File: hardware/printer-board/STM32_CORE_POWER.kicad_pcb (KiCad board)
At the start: 2 copper layers, 9 parts, among them J46 Conn_01x03, U14 AMS1117-3.3

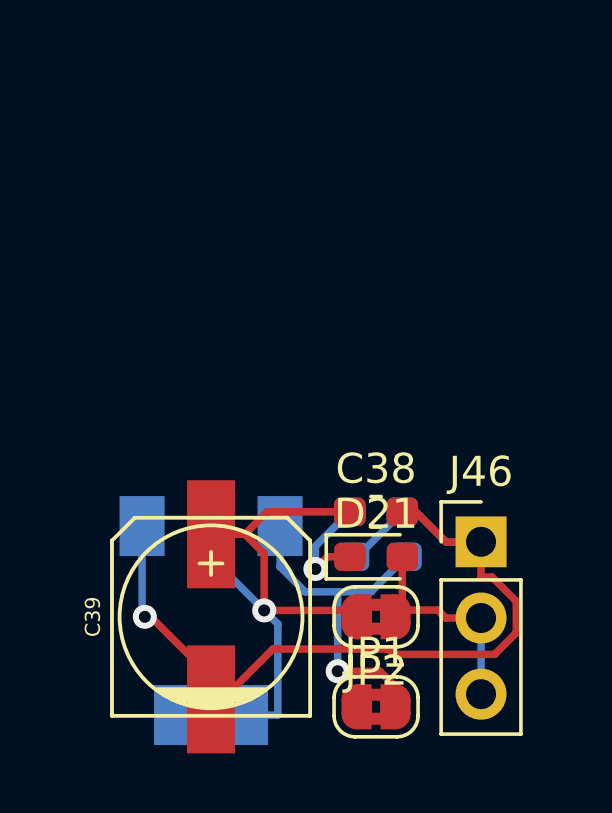
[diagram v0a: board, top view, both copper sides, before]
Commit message: update power circuit,
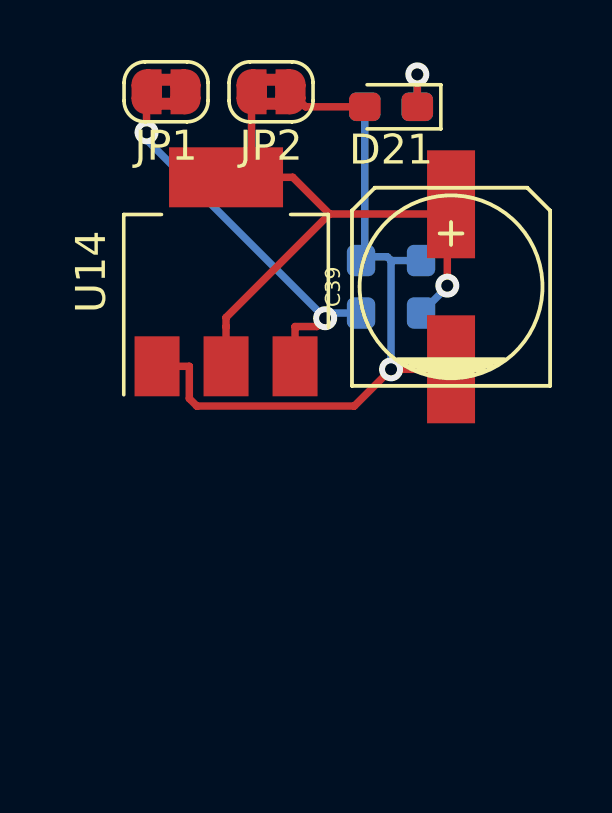
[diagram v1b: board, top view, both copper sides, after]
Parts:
- removed J46: Conn_01x03, Connector_PinHeader_2.54mm:PinHeader_1x03_P2.54mm_Vertical
- C38: moved to B.Cu
- D21: value LED_GREEN,0603 -> 3v3 HEALTHY
- U14: moved to F.Cu
- moved JP1 21.7 mm to (17.5, 16.5), turned to 180 degrees
- moved JP2 17.8 mm to (21.0, 16.5)
- moved D21 15.0 mm to (25.0, 17.0), turned to 180 degrees
- moved C39 13.6 mm to (27.0, 23.0)
- moved R65 13.5 mm to (25.0, 17.0), turned to 180 degrees
- moved U14 11.6 mm to (19.5, 22.5), turned to 90 degrees
- moved C37 9.02 mm to (24.0, 23.0), turned to 90 degrees
- moved C38 7.65 mm to (26.0, 23.0), turned to 90 degrees
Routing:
- net GND: track 30.3 -> 22.2 mm
- net +3V3: track 7.37 -> 2.68 mm
- net Net-(C37-Pad1): track 11.8 -> 13.7 mm, vias 1 -> 2
- net Net-(D21-Pad1): track 3.70 -> 2.16 mm
- net Net-(C38-Pad1): track 20.5 -> 21.4 mm

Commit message: update for stepper Z,
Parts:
- removed U14: AMS1117-3.3, Package_TO_SOT_SMD:SOT-223-3_TabPin2
- added C1: CP100uf,35V, Capacitor_SMD:C_0603_1608Metric_Pad1.05x0.95mm_HandSolder, F.Cu at (190.6, 45.3)
- added C10: CP100uf,25V, Capacitor_SMD:CP_Elec_6.3x7.7, F.Cu at (297.3, 53.2)
- added C11: C104,0603, Capacitor_SMD:C_0603_1608Metric_Pad1.05x0.95mm_HandSolder, F.Cu at (297.6, 59.1)
- added C12: CP100uf,25V, Capacitor_SMD:CP_Elec_6.3x7.7, F.Cu at (240.3, 109.1)
- added C13: C104,0603, Capacitor_SMD:C_0603_1608Metric_Pad1.05x0.95mm_HandSolder, F.Cu at (237.3, 115.0)
- added C14: C106,0603, Capacitor_SMD:C_0603_1608Metric_Pad1.05x0.95mm_HandSolder, F.Cu at (295.6, 127.7)
- added C15: C106,0603, Capacitor_SMD:C_0603_1608Metric_Pad1.05x0.95mm_HandSolder, F.Cu at (292.3, 136.8)
- added C16: C106,0603, Capacitor_SMD:C_0603_1608Metric_Pad1.05x0.95mm_HandSolder, F.Cu at (292.3, 127.7)
- added C17: C106,0603, Capacitor_SMD:C_0603_1608Metric_Pad1.05x0.95mm_HandSolder, F.Cu at (295.6, 129.2)
- added C18: C106,0603, Capacitor_SMD:C_0603_1608Metric_Pad1.05x0.95mm_HandSolder, F.Cu at (292.3, 132.3)
- added C19: C104,0603, Capacitor_SMD:C_0603_1608Metric_Pad1.05x0.95mm_HandSolder, F.Cu at (221.4, 140.3)
- added C2: CP100uf,25V, Capacitor_SMD:CP_Elec_6.3x7.7, F.Cu at (160.0, 109.1)
- added C20: CP100uf,35V, Capacitor_SMD:CP_Elec_6.3x7.7, F.Cu at (235.1, 137.6)
- added C21: C104,0603, Capacitor_SMD:C_0603_1608Metric_Pad1.05x0.95mm_HandSolder, F.Cu at (295.3, 86.0)
- added C22: C10pf,0603, Capacitor_SMD:C_0603_1608Metric_Pad1.05x0.95mm_HandSolder, F.Cu at (281.9, 85.8)
- added C23: C104,0603, Capacitor_SMD:C_0603_1608Metric_Pad1.05x0.95mm_HandSolder, F.Cu at (308.3, 76.8)
- added C24: C10pf,0603, Capacitor_SMD:C_0603_1608Metric_Pad1.05x0.95mm_HandSolder, F.Cu at (285.2, 85.8)
- added C25: C104,0603, Capacitor_SMD:C_0603_1608Metric_Pad1.05x0.95mm_HandSolder, F.Cu at (295.1, 82.0)
- added C26: C104,0603, Capacitor_SMD:C_0603_1608Metric_Pad1.05x0.95mm_HandSolder, F.Cu at (295.1, 80.4)
- added C27: C104,0603, Capacitor_SMD:C_0603_1608Metric_Pad1.05x0.95mm_HandSolder, F.Cu at (298.5, 80.4)
- added C28: C104,0603, Capacitor_SMD:C_0603_1608Metric_Pad1.05x0.95mm_HandSolder, F.Cu at (295.1, 83.5)
- added C29: C105,0603, Capacitor_SMD:C_0603_1608Metric_Pad1.05x0.95mm_HandSolder, F.Cu at (305.0, 75.3)
- added C3: C104,0603, Capacitor_SMD:C_0603_1608Metric_Pad1.05x0.95mm_HandSolder, F.Cu at (166.4, 109.9)
- added C30: C104,0603, Capacitor_SMD:C_0603_1608Metric_Pad1.05x0.95mm_HandSolder, F.Cu at (298.5, 78.9)
- added C31: C104,0603, Capacitor_SMD:C_0603_1608Metric_Pad1.05x0.95mm_HandSolder, F.Cu at (291.9, 85.8)
- added C32: C104,0603, Capacitor_SMD:C_0603_1608Metric_Pad1.05x0.95mm_HandSolder, F.Cu at (288.6, 85.8)
- added C33: CP220uf,16V, Capacitor_SMD:C_0603_1608Metric_Pad1.05x0.95mm_HandSolder, F.Cu at (147.7, 149.0)
- added C34: CP220uf,16V, Capacitor_SMD:C_0603_1608Metric_Pad1.05x0.95mm_HandSolder, F.Cu at (144.3, 149.0)
- added C35: CP220uf,25V, Capacitor_SMD:C_0603_1608Metric_Pad1.05x0.95mm_HandSolder, F.Cu at (144.3, 150.5)
- added C36: CP100uf,16V, Capacitor_SMD:CP_Elec_6.3x5.3, F.Cu at (259.2, 130.5)
- added C4: CP100uf,25V, Capacitor_SMD:CP_Elec_6.3x7.7, F.Cu at (200.2, 109.1)
- added C40: C104,0603, Capacitor_SMD:C_0603_1608Metric_Pad1.05x0.95mm_HandSolder, F.Cu at (254.2, 84.5)
- added C41: CP100uf,25V, Capacitor_SMD:CP_Elec_6.3x7.7, F.Cu at (257.2, 53.2)
- added C42: C104,0603, Capacitor_SMD:C_0603_1608Metric_Pad1.05x0.95mm_HandSolder, F.Cu at (263.6, 54.0)
- added C43: C104,0603, Capacitor_SMD:C_0603_1608Metric_Pad1.05x0.95mm_HandSolder, F.Cu at (274.0, 103.0)
- added C44: CP100uf,16V, Capacitor_SMD:CP_Elec_6.3x5.3, F.Cu at (280.3, 95.8)
- added C45: C106,0603, Capacitor_SMD:C_0603_1608Metric_Pad1.05x0.95mm_HandSolder, F.Cu at (318.6, 92.3)
- added C46: C104,0603, Capacitor_SMD:C_0603_1608Metric_Pad1.05x0.95mm_HandSolder, F.Cu at (325.3, 92.3)
- added C47: C332,0603, Capacitor_SMD:C_0603_1608Metric_Pad1.05x0.95mm_HandSolder, F.Cu at (322.0, 92.3)
- added C48: C103,0603, Capacitor_SMD:C_0603_1608Metric_Pad1.05x0.95mm_HandSolder, F.Cu at (318.6, 93.8)
- added C49: C226,6.3v,0603, Capacitor_SMD:C_0603_1608Metric_Pad1.05x0.95mm_HandSolder, F.Cu at (328.7, 93.8)
- added C5: C104,0603, Capacitor_SMD:C_0603_1608Metric_Pad1.05x0.95mm_HandSolder, F.Cu at (197.2, 116.6)
- added C50: C106,0603, Capacitor_SMD:C_0603_1608Metric_Pad1.05x0.95mm_HandSolder, F.Cu at (224.8, 152.9)
- added C51: C104,0603, Capacitor_SMD:C_0603_1608Metric_Pad1.05x0.95mm_HandSolder, F.Cu at (228.1, 151.4)
- added C52: C332,0603, Capacitor_SMD:C_0603_1608Metric_Pad1.05x0.95mm_HandSolder, F.Cu at (221.4, 152.9)
- added C53: C103,0603, Capacitor_SMD:C_0603_1608Metric_Pad1.05x0.95mm_HandSolder, F.Cu at (224.8, 151.4)
- added C54: C226,6.3v,0603, Capacitor_SMD:C_0603_1608Metric_Pad1.05x0.95mm_HandSolder, F.Cu at (221.4, 151.4)
- added C6: CP100uf,25V, Capacitor_SMD:CP_Elec_6.3x7.7, F.Cu at (160.0, 133.1)
- added C7: C104,0603, Capacitor_SMD:C_0603_1608Metric_Pad1.05x0.95mm_HandSolder, F.Cu at (160.3, 139.0)
- added C8: CP100uf,25V, Capacitor_SMD:CP_Elec_6.3x7.7, F.Cu at (200.1, 133.1)
- added C9: C104,0603, Capacitor_SMD:C_0603_1608Metric_Pad1.05x0.95mm_HandSolder, F.Cu at (197.1, 140.5)
- added D1: 5V HEALTHY, LED_SMD:LED_0603_1608Metric_Pad1.05x0.95mm_HandSolder, F.Cu at (141.2, 93.6)
- added D10: LED_BLUE,0603, LED_SMD:LED_0603_1608Metric_Pad1.05x0.95mm_HandSolder, F.Cu at (315.2, 79.3)
- added D11: LED_BLUE,0603, LED_SMD:LED_0603_1608Metric_Pad1.05x0.95mm_HandSolder, F.Cu at (318.6, 79.3)
- added D12: LED_BLUE,0603, LED_SMD:LED_0603_1608Metric_Pad1.05x0.95mm_HandSolder, F.Cu at (318.6, 80.9)
- added D13: LED_BLUE,0603, LED_SMD:LED_0603_1608Metric_Pad1.05x0.95mm_HandSolder, F.Cu at (325.4, 79.3)
- added D14: LED_BLUE,0603, LED_SMD:LED_0603_1608Metric_Pad1.05x0.95mm_HandSolder, F.Cu at (322.0, 79.3)
- added D15: SD_M4, Diode_SMD:D_SOD-323_HandSoldering, F.Cu at (221.8, 136.1)
- added D16: SD_M4, Diode_SMD:D_SOD-323_HandSoldering, F.Cu at (225.8, 136.1)
- added D17: PB9, LED_SMD:LED_0603_1608Metric_Pad1.05x0.95mm_HandSolder, F.Cu at (278.5, 85.8)
- added D18: LED_RED,0603, LED_SMD:LED_0603_1608Metric_Pad1.05x0.95mm_HandSolder, F.Cu at (295.3, 102.5)
- added D19: LED_RED,0603, LED_SMD:LED_0603_1608Metric_Pad1.05x0.95mm_HandSolder, F.Cu at (265.4, 122.5)
- added D2: LED_BLUE,0603, LED_SMD:LED_0603_1608Metric_Pad1.05x0.95mm_HandSolder, F.Cu at (157.0, 115.4)
- added D20: LED_BLUE,0603, LED_SMD:LED_0603_1608Metric_Pad1.05x0.95mm_HandSolder, F.Cu at (259.8, 134.9)
- added D22: LED_BLUE,0603, LED_SMD:LED_0603_1608Metric_Pad1.05x0.95mm_HandSolder, F.Cu at (272.1, 142.3)
- added D23: LED_BLUE,0603, LED_SMD:LED_0603_1608Metric_Pad1.05x0.95mm_HandSolder, F.Cu at (254.2, 81.4)
- added D24: LED_BLUE,0603, LED_SMD:LED_0603_1608Metric_Pad1.05x0.95mm_HandSolder, F.Cu at (254.2, 57.5)
- added D3: LED_BLUE,0603, LED_SMD:LED_0603_1608Metric_Pad1.05x0.95mm_HandSolder, F.Cu at (197.2, 113.5)
- added D4: LED_BLUE,0603, LED_SMD:LED_0603_1608Metric_Pad1.05x0.95mm_HandSolder, F.Cu at (157.0, 137.4)
- added D5: LED_BLUE,0603, LED_SMD:LED_0603_1608Metric_Pad1.05x0.95mm_HandSolder, F.Cu at (197.1, 137.4)
- added D6: LED_BLUE,0603, LED_SMD:LED_0603_1608Metric_Pad1.05x0.95mm_HandSolder, F.Cu at (294.3, 57.5)
- added D7: LED_BLUE,0603, LED_SMD:LED_0603_1608Metric_Pad1.05x0.95mm_HandSolder, F.Cu at (237.3, 113.5)
- added D8: LED_RED,0603, LED_SMD:LED_0603_1608Metric_Pad1.05x0.95mm_HandSolder, F.Cu at (295.3, 119.1)
- added D9: LED_BLUE,0603, LED_SMD:LED_0603_1608Metric_Pad1.05x0.95mm_HandSolder, F.Cu at (315.2, 80.9)
- added F1: 16V/30A, w_misc_comp:fuse_smf, F.Cu at (225.0, 127.0)
- added F2: 30V/5A, w_misc_comp:fuse_smf, F.Cu at (225.0, 132.4)
- added H1: MOUNT_M3, MountingHole:MountingHole_2.7mm_M2.5, F.Cu at (3.00, 3.00)
- added H2: MOUNT_M3, MountingHole:MountingHole_2.7mm_M2.5, F.Cu at (97.0, 3.00)
- added H3: MOUNT_M3, MountingHole:MountingHole_2.7mm_M2.5, F.Cu at (3.00, 97.0)
- added H4: MOUNT_M3, MountingHole:MountingHole_2.7mm_M2.5, F.Cu at (97.0, 97.0)
- added J1: USB_DEBUG, Connector_PinHeader_1.27mm:PinHeader_1x05_P1.27mm_Vertical, F.Cu at (187.4, 45.7)
- added J10: MS_SELECT, Connector_PinHeader_2.54mm:PinHeader_2x03_P2.54mm_Vertical, F.Cu at (304.8, 46.3)
- added J11: E0, footprint-lib:b4b-ph-kl,stepper_terminal, F.Cu at (297.8, 46.6)
- added J12: MS_SELECT, Connector_PinHeader_2.54mm:PinHeader_2x03_P2.54mm_Vertical, F.Cu at (247.8, 102.3)
- added J13: E1, footprint-lib:b4b-ph-kl,stepper_terminal, F.Cu at (240.8, 102.6)
- added J14: HEATBED, footprint-lib:mpt_0,5%2f2-2,54,heatbed, F.Cu at (309.5, 113.4)
- added J15: X_MIN, footprint-lib:b3b-ph-kl,end_stop, F.Cu at (317.7, 70.5)
- added J16: X_MAX, footprint-lib:b3b-ph-kl,end_stop, F.Cu at (317.7, 75.6)
- added J17: Y_MIN, footprint-lib:b3b-ph-kl,end_stop, F.Cu at (326.1, 70.5)
- added J18: Y_MAX, footprint-lib:b3b-ph-kl,end_stop, F.Cu at (326.1, 75.6)
- added J19: Z_MIN, footprint-lib:b3b-ph-kl,end_stop, F.Cu at (334.5, 70.5)
- added J2: MS_SELECT, Connector_PinHeader_2.54mm:PinHeader_2x03_P2.54mm_Vertical, F.Cu at (167.5, 102.3)
- added J20: Z_MAX, footprint-lib:b3b-ph-kl,end_stop, F.Cu at (334.5, 75.6)
- added J21: HEATBED_TEMP, w_conn_jst-ph:b2b-ph-kl, F.Cu at (281.1, 134.1)
- added J22: HOTEND_TEMP0, w_conn_jst-ph:b2b-ph-kl, F.Cu at (281.1, 129.1)
- added J23: HOTEND_TEMP1, w_conn_jst-ph:b2b-ph-kl, F.Cu at (287.4, 129.1)
- added J24: AUX_TEMP, w_conn_jst-ph:b2b-ph-kl, F.Cu at (287.4, 134.1)
- added J25: 12V_INPUT_2, footprint-lib:mpt_0,5%2f2-2,54,12V_SRC, F.Cu at (245.3, 130.8)
- added J26: 12V_INPUT, footprint-lib:mpt_0,5%2f2-2,54,12V_SRC, F.Cu at (239.3, 130.8)
- added J27: 12V_OUT, footprint-lib:mpt_0,5%2f2-2,54,12V_SRC, F.Cu at (233.3, 130.8)
- added J28: SWD, Connector_PinHeader_1.27mm:PinHeader_1x04_P1.27mm_Vertical, F.Cu at (307.2, 69.6)
- added J29: USB_DEBUG, Connector_PinHeader_1.27mm:PinHeader_1x05_P1.27mm_Vertical, F.Cu at (157.4, 149.5)
- added J3: X, footprint-lib:b4b-ph-kl,stepper_terminal, F.Cu at (160.5, 102.6)
- added J30: PWR_DEBUG, Connector_PinHeader_1.27mm:PinHeader_1x05_P1.27mm_Vertical, F.Cu at (141.1, 149.5)
- added J31: HOT_END, footprint-lib:mpt_0,5%2f2-2,54,heatbed, F.Cu at (309.5, 96.8)
- added J32: HOT_END, footprint-lib:mpt_0,5%2f2-2,54,heatbed, F.Cu at (279.6, 116.8)
- added J33: TO FAN0, footprint-lib:b2b-ph-kl,fan_pwm_out, F.Cu at (267.2, 129.1)
- added J34: TO FAN1, footprint-lib:b2b-ph-kl,fan_pwm_out, F.Cu at (329.8, 46.6)
- added J35: TO FAN2, footprint-lib:b2b-ph-kl,fan_pwm_out, F.Cu at (267.2, 143.6)
- added J36: MS_SELECT, Connector_PinHeader_2.54mm:PinHeader_2x03_P2.54mm_Vertical, F.Cu at (264.7, 70.2)
- added J37: Z2, footprint-lib:b4b-ph-kl,stepper_terminal, F.Cu at (257.7, 70.5)
- added J38: MS_SELECT, Connector_PinHeader_2.54mm:PinHeader_2x03_P2.54mm_Vertical, F.Cu at (264.7, 46.3)
- added J39: Y, footprint-lib:b4b-ph-kl,stepper_terminal, F.Cu at (257.7, 46.6)
- added J4: MS_SELECT, Connector_PinHeader_2.54mm:PinHeader_2x03_P2.54mm_Vertical, F.Cu at (207.7, 102.3)
- added J40: Conn_01x07, Connector_PinHeader_1.27mm:PinHeader_1x07_P1.27mm_Vertical, F.Cu at (273.9, 93.4)
- added J41: EXP1, Connector_PinHeader_2.54mm:PinHeader_2x05_P2.54mm_Vertical, F.Cu at (261.8, 94.1)
- added J42: EXP2, Connector_PinHeader_2.54mm:PinHeader_2x05_P2.54mm_Vertical, F.Cu at (268.0, 94.1)
- added J5: Z, footprint-lib:b4b-ph-kl,stepper_terminal, F.Cu at (200.7, 102.6)
- added J6: MS_SELECT, Connector_PinHeader_2.54mm:PinHeader_2x03_P2.54mm_Vertical, F.Cu at (167.5, 126.2)
- added J7: Z1, footprint-lib:b4b-ph-kl,stepper_terminal, F.Cu at (160.5, 126.5)
- added J8: MS_SELECT, Connector_PinHeader_2.54mm:PinHeader_2x03_P2.54mm_Vertical, F.Cu at (207.6, 126.2)
- added J9: Z3, footprint-lib:b4b-ph-kl,stepper_terminal, F.Cu at (200.6, 126.5)
- added JP3: Jumper_NO_Small, Jumper:SolderJumper-2_P1.3mm_Open_TrianglePad1.0x1.5mm, F.Cu at (194.0, 45.8)
- added JP4: Jumper_NO_Small, Jumper:SolderJumper-2_P1.3mm_Open_TrianglePad1.0x1.5mm, F.Cu at (144.6, 94.1)
- added JP5: Jumper_NO_Small, SolderJumper-2_P1.3mm_Open_TrianglePad1.0x1.5mm, F.Cu at (221.4, 138.3)
- added JP6: Jumper_NO_Small, SolderJumper-2_P1.3mm_Open_TrianglePad1.0x1.5mm, F.Cu at (298.5, 84.0)
- added JP7: Jumper_NO_Small, SolderJumper-2_P1.3mm_Open_TrianglePad1.0x1.5mm, F.Cu at (305.2, 78.8)
- added L1: L_Small, w_smd_inductors:inductor_smd_0603, F.Cu at (301.3, 83.4)
- added L2: L_15uH, w_smd_inductors:inductor_smd_4.8x2.8mm, F.Cu at (327.2, 88.8)
- added L3: L_15uH, w_smd_inductors:inductor_smd_4.8x2.8mm, F.Cu at (229.9, 147.9)
- added Q1: WSK220N04, footprint-lib:TO-263-2,drill_array, F.Cu at (298.1, 112.6)
- added Q2: STP55NF06, footprint-lib:TO-263-2,drill_array, F.Cu at (298.1, 96.0)
- added Q3: STP55NF06, footprint-lib:TO-263-2,drill_array, F.Cu at (268.3, 116.0)
- added Q4: D882, footprint-lib:SOT-89-3,thermal_vias, F.Cu at (266.5, 134.6)
- added Q5: D882, footprint-lib:SOT-89-3,thermal_vias, F.Cu at (329.1, 52.2)
- added Q6: D882, footprint-lib:SOT-89-3,thermal_vias, F.Cu at (266.5, 149.2)
- added R1: R153,0603, Resistor_SMD:R_0603_1608Metric_Pad1.05x0.95mm_HandSolder, F.Cu at (238.4, 94.5)
- added R10: R103,0603, Resistor_SMD:R_0603_1608Metric_Pad1.05x0.95mm_HandSolder, F.Cu at (160.4, 115.4)
- added R11: R104,0603, Resistor_SMD:R_0603_1608Metric_Pad1.05x0.95mm_HandSolder, F.Cu at (197.2, 115.0)
- added R12: R102,0603, Resistor_SMD:R_0603_1608Metric_Pad1.05x0.95mm_HandSolder, F.Cu at (206.6, 109.9)
- added R13: R103,0603, Resistor_SMD:R_0603_1608Metric_Pad1.05x0.95mm_HandSolder, F.Cu at (200.5, 115.0)
- added R14: R104,0603, Resistor_SMD:R_0603_1608Metric_Pad1.05x0.95mm_HandSolder, F.Cu at (166.4, 133.9)
- added R15: R102,0603, Resistor_SMD:R_0603_1608Metric_Pad1.05x0.95mm_HandSolder, F.Cu at (157.0, 139.0)
- added R16: R103,0603, Resistor_SMD:R_0603_1608Metric_Pad1.05x0.95mm_HandSolder, F.Cu at (157.0, 140.5)
- added R17: R104,0603, Resistor_SMD:R_0603_1608Metric_Pad1.05x0.95mm_HandSolder, F.Cu at (197.1, 139.0)
- added R18: R102,0603, Resistor_SMD:R_0603_1608Metric_Pad1.05x0.95mm_HandSolder, F.Cu at (206.5, 133.9)
- added R19: R103,0603, Resistor_SMD:R_0603_1608Metric_Pad1.05x0.95mm_HandSolder, F.Cu at (200.4, 139.0)
- added R2: R153,0603, Resistor_SMD:R_0603_1608Metric_Pad1.05x0.95mm_HandSolder, F.Cu at (238.4, 93.0)
- added R20: R104,0603, Resistor_SMD:R_0603_1608Metric_Pad1.05x0.95mm_HandSolder, F.Cu at (303.7, 54.0)
- added R21: R102,0603, Resistor_SMD:R_0603_1608Metric_Pad1.05x0.95mm_HandSolder, F.Cu at (294.3, 60.6)
- added R22: R103,0603, Resistor_SMD:R_0603_1608Metric_Pad1.05x0.95mm_HandSolder, F.Cu at (294.3, 59.1)
- added R23: R104,0603, Resistor_SMD:R_0603_1608Metric_Pad1.05x0.95mm_HandSolder, F.Cu at (240.6, 115.0)
- added R24: R102,0603, Resistor_SMD:R_0603_1608Metric_Pad1.05x0.95mm_HandSolder, F.Cu at (246.7, 109.9)
- added R25: R103,0603, Resistor_SMD:R_0603_1608Metric_Pad1.05x0.95mm_HandSolder, F.Cu at (237.3, 116.6)
- added R26: R100,0805, Resistor_SMD:R_0805_2012Metric_Pad1.15x1.40mm_HandSolder, F.Cu at (308.3, 117.6)
- added R27: R104,0805, Resistor_SMD:R_0805_2012Metric_Pad1.15x1.40mm_HandSolder, F.Cu at (291.7, 119.3)
- added R28: R182,0603, Resistor_SMD:R_0603_1608Metric_Pad1.05x0.95mm_HandSolder, F.Cu at (298.6, 119.0)
- added R29: R102,0603, Resistor_SMD:R_0603_1608Metric_Pad1.05x0.95mm_HandSolder, F.Cu at (332.0, 82.3)
- added R3: R152,0603, Resistor_SMD:R_0603_1608Metric_Pad1.05x0.95mm_HandSolder, F.Cu at (241.7, 93.0)
- added R30: R102,0603, Resistor_SMD:R_0603_1608Metric_Pad1.05x0.95mm_HandSolder, F.Cu at (328.7, 79.3)
- added R31: R102,0603, Resistor_SMD:R_0603_1608Metric_Pad1.05x0.95mm_HandSolder, F.Cu at (325.3, 80.9)
- added R32: R102,0603, Resistor_SMD:R_0603_1608Metric_Pad1.05x0.95mm_HandSolder, F.Cu at (328.7, 80.8)
- added R33: R102,0603, Resistor_SMD:R_0603_1608Metric_Pad1.05x0.95mm_HandSolder, F.Cu at (328.7, 82.3)
- added R34: R102,0603, Resistor_SMD:R_0603_1608Metric_Pad1.05x0.95mm_HandSolder, F.Cu at (322.0, 80.9)
- added R35: R472,0603, Resistor_SMD:R_0603_1608Metric_Pad1.05x0.95mm_HandSolder, F.Cu at (292.3, 129.2)
- added R36: R472,0603, Resistor_SMD:R_0603_1608Metric_Pad1.05x0.95mm_HandSolder, F.Cu at (292.3, 130.7)
- added R37: R472,0603, Resistor_SMD:R_0603_1608Metric_Pad1.05x0.95mm_HandSolder, F.Cu at (292.3, 135.3)
- added R38: R472,0603, Resistor_SMD:R_0603_1608Metric_Pad1.05x0.95mm_HandSolder, F.Cu at (295.6, 132.3)
- added R39: R472,0603, Resistor_SMD:R_0603_1608Metric_Pad1.05x0.95mm_HandSolder, F.Cu at (292.3, 133.8)
- added R4: R220,0603, Resistor_SMD:R_0603_1608Metric_Pad1.05x0.95mm_HandSolder, F.Cu at (187.5, 52.7)
- added R40: R472,0603, Resistor_SMD:R_0603_1608Metric_Pad1.05x0.95mm_HandSolder, F.Cu at (301.8, 82.0)
- added R41: R472,0603, Resistor_SMD:R_0603_1608Metric_Pad1.05x0.95mm_HandSolder, F.Cu at (301.8, 80.4)
- added R42: R0,0603, Resistor_SMD:R_0603_1608Metric_Pad1.05x0.95mm_HandSolder, F.Cu at (308.3, 75.3)
- added R43: R0,0603, Resistor_SMD:R_0603_1608Metric_Pad1.05x0.95mm_HandSolder, F.Cu at (295.1, 78.9)
- added R44: R102,0603, Resistor_SMD:R_0603_1608Metric_Pad1.05x0.95mm_HandSolder, F.Cu at (301.8, 78.9)
- added R45: R103,0603, Resistor_SMD:R_0603_1608Metric_Pad1.05x0.95mm_HandSolder, F.Cu at (305.0, 76.8)
- added R46: R103,0603, Resistor_SMD:R_0603_1608Metric_Pad1.05x0.95mm_HandSolder, F.Cu at (298.5, 82.0)
- added R47: R220,0603, Resistor_SMD:R_0603_1608Metric_Pad1.05x0.95mm_HandSolder, F.Cu at (160.7, 150.5)
- added R48: R220,0603, Resistor_SMD:R_0603_1608Metric_Pad1.05x0.95mm_HandSolder, F.Cu at (164.0, 149.0)
- added R49: R152,0603, Resistor_SMD:R_0603_1608Metric_Pad1.05x0.95mm_HandSolder, F.Cu at (160.7, 149.0)
- added R5: R220,0603, Resistor_SMD:R_0603_1608Metric_Pad1.05x0.95mm_HandSolder, F.Cu at (147.9, 93.6)
- added R50: R100,0805, Resistor_SMD:R_0805_2012Metric_Pad1.15x1.40mm_HandSolder, F.Cu at (308.3, 101.0)
- added R51: R104,0805, Resistor_SMD:R_0805_2012Metric_Pad1.15x1.40mm_HandSolder, F.Cu at (291.7, 102.7)
- added R52: R182,0603, Resistor_SMD:R_0603_1608Metric_Pad1.05x0.95mm_HandSolder, F.Cu at (298.6, 102.4)
- added R53: R100,0805, Resistor_SMD:R_0805_2012Metric_Pad1.15x1.40mm_HandSolder, F.Cu at (261.8, 122.7)
- added R54: R104,0805, Resistor_SMD:R_0805_2012Metric_Pad1.15x1.40mm_HandSolder, F.Cu at (278.5, 121.0)
- added R55: R182,0603, Resistor_SMD:R_0603_1608Metric_Pad1.05x0.95mm_HandSolder, F.Cu at (268.8, 122.5)
- added R56: R100,0805, Resistor_SMD:R_0805_2012Metric_Pad1.15x1.40mm_HandSolder, F.Cu at (272.3, 127.9)
- added R57: R104,0805, Resistor_SMD:R_0805_2012Metric_Pad1.15x1.40mm_HandSolder, F.Cu at (256.2, 135.1)
- added R58: R100,0603, Resistor_SMD:R_0603_1608Metric_Pad1.05x0.95mm_HandSolder, F.Cu at (259.4, 136.8)
- added R59: R182,0603, Resistor_SMD:R_0603_1608Metric_Pad1.05x0.95mm_HandSolder, F.Cu at (256.0, 136.8)
- added R6: R152,0603, Resistor_SMD:R_0603_1608Metric_Pad1.05x0.95mm_HandSolder, F.Cu at (190.6, 48.3)
- added R60: R100,0805, Resistor_SMD:R_0805_2012Metric_Pad1.15x1.40mm_HandSolder, F.Cu at (334.8, 45.5)
- added R61: R104,0805, Resistor_SMD:R_0805_2012Metric_Pad1.15x1.40mm_HandSolder, F.Cu at (318.8, 52.6)
- added R62: R100,0603, Resistor_SMD:R_0603_1608Metric_Pad1.05x0.95mm_HandSolder, F.Cu at (318.6, 54.4)
- added R63: R182,0603, Resistor_SMD:R_0603_1608Metric_Pad1.05x0.95mm_HandSolder, F.Cu at (322.0, 54.4)
- added R64: R100,0805, Resistor_SMD:R_0603_1608Metric_Pad1.05x0.95mm_HandSolder, F.Cu at (259.8, 149.4)
- added R66: R100,0603, Resistor_SMD:R_0603_1608Metric_Pad1.05x0.95mm_HandSolder, F.Cu at (256.0, 151.4)
- added R67: R182,0603, Resistor_SMD:R_0603_1608Metric_Pad1.05x0.95mm_HandSolder, F.Cu at (259.4, 151.4)
- added R68: R104,0603, Resistor_SMD:R_0603_1608Metric_Pad1.05x0.95mm_HandSolder, F.Cu at (257.5, 83.0)
- added R69: R102,0603, Resistor_SMD:R_0603_1608Metric_Pad1.05x0.95mm_HandSolder, F.Cu at (254.2, 83.0)
- added R7: R102,0603, Resistor_SMD:R_0603_1608Metric_Pad1.05x0.95mm_HandSolder, F.Cu at (190.6, 46.8)
- added R70: R103,0603, Resistor_SMD:R_0603_1608Metric_Pad1.05x0.95mm_HandSolder, F.Cu at (263.6, 77.8)
- added R71: R104,0603, Resistor_SMD:R_0603_1608Metric_Pad1.05x0.95mm_HandSolder, F.Cu at (257.5, 59.1)
- added R72: R102,0603, Resistor_SMD:R_0603_1608Metric_Pad1.05x0.95mm_HandSolder, F.Cu at (254.2, 60.6)
- added R73: R103,0603, Resistor_SMD:R_0603_1608Metric_Pad1.05x0.95mm_HandSolder, F.Cu at (254.2, 59.1)
- added R74: R562,0603, Resistor_SMD:R_0603_1608Metric_Pad1.05x0.95mm_HandSolder, F.Cu at (328.7, 92.3)
- added R75: R103,0603, Resistor_SMD:R_0603_1608Metric_Pad1.05x0.95mm_HandSolder, F.Cu at (325.3, 93.8)
- added R76: R333,0603, Resistor_SMD:R_0603_1608Metric_Pad1.05x0.95mm_HandSolder, F.Cu at (322.0, 93.8)
- added R77: R562,0603, Resistor_SMD:R_0603_1608Metric_Pad1.05x0.95mm_HandSolder, F.Cu at (228.1, 152.9)
- added R78: R103,0603, Resistor_SMD:R_0603_1608Metric_Pad1.05x0.95mm_HandSolder, F.Cu at (231.5, 151.4)
- added R79: R333,0603, Resistor_SMD:R_0603_1608Metric_Pad1.05x0.95mm_HandSolder, F.Cu at (231.5, 152.9)
- added R8: R104,0603, Resistor_SMD:R_0805_2012Metric_Pad1.15x1.40mm_HandSolder, F.Cu at (157.2, 113.7)
- added R9: R102,0603, Resistor_SMD:R_0603_1608Metric_Pad1.05x0.95mm_HandSolder, F.Cu at (157.0, 117.0)
- added SW1: SW_Push, Button_Switch_SMD:SW_SPST_CK_RS282G05A3, F.Cu at (298.4, 76.1)
- added TH1: Thermistor_NTC, Resistor_SMD:R_0603_1608Metric_Pad1.05x0.95mm_HandSolder, F.Cu at (295.6, 130.7)
- added U1: orange_pi_zero, footprint-lib:orangepi-zero, F.Cu at (139.8, 92.6)
- added U10: A4988_MODULE, footprint-lib:Pololu_Breakout-16_15.2x20.3mm, F.Cu at (238.2, 46.0)
- added U11: MP2303A_ALT, footprint-lib:SOIC-8_3.9x4.9mm_P1.27mm,thermal_via, F.Cu at (320.7, 88.8)
- added U12: MP2303A_ALT, footprint-lib:SOIC-8_3.9x4.9mm_P1.27mm,thermal_via, F.Cu at (223.5, 147.9)
- added U2: A4988_MODULE, footprint-lib:Pololu_Breakout-16_15.2x20.3mm, F.Cu at (141.1, 102.0)
- added U3: A4988_MODULE, footprint-lib:Pololu_Breakout-16_15.2x20.3mm, F.Cu at (181.3, 102.0)
- added U4: A4988_MODULE, footprint-lib:Pololu_Breakout-16_15.2x20.3mm, F.Cu at (141.1, 125.9)
- added U5: A4988_MODULE, footprint-lib:Pololu_Breakout-16_15.2x20.3mm, F.Cu at (181.2, 125.9)
- added U6: A4988_MODULE, footprint-lib:Pololu_Breakout-16_15.2x20.3mm, F.Cu at (278.4, 46.0)
- added U7: A4988_MODULE, footprint-lib:Pololu_Breakout-16_15.2x20.3mm, F.Cu at (221.4, 102.0)
- added U8: STM32F407VET6, w_smd_lqfp:TQFP-100, F.Cu at (285.1, 76.7)
- added U9: A4988_MODULE, footprint-lib:Pololu_Breakout-16_15.2x20.3mm, F.Cu at (238.2, 69.9)
- added Y1: O_8M, Crystal:Crystal_HC49-4H_Vertical, F.Cu at (297.1, 71.2)
- C37, C38: value C104,0603 -> CP100uf,16V; footprint Capacitor_SMD:C_0603_1608Metric_Pad1.05x0.95mm_HandSolder -> Capacitor_SMD:CP_Elec_6.3x5.3; moved to F.Cu
- C39: value CP47uf,50V -> CP100uf,25V; footprint w_smd_cap:c_elec_6.3x7.7 -> Capacitor_SMD:CP_Elec_6.3x7.7
- D21: value 3v3 HEALTHY -> LED_BLUE,0603
- JP1, JP2: footprint Jumper:SolderJumper-2_P1.3mm_Bridged2Bar_RoundedPad1.0x1.5mm -> Jumper:SolderJumper-2_P1.3mm_Open_TrianglePad1.0x1.5mm
- R65: value R102,0603 -> R104,0805; footprint Resistor_SMD:R_0603_1608Metric_Pad1.05x0.95mm_HandSolder -> Resistor_SMD:R_0805_2012Metric_Pad1.15x1.40mm_HandSolder; moved to F.Cu
- moved D21 299.5 mm to (322.4, 52.4), turned to 0 degrees
- moved C37 298.8 mm to (321.8, 48.1), turned to 0 degrees
- moved R65 266.6 mm to (256.2, 149.6), turned to 0 degrees
- moved C38 263.2 mm to (259.2, 145.1), turned to 0 degrees
- moved C39 236.5 mm to (257.2, 77.0), turned to 0 degrees
- moved JP2 170.8 mm to (187.5, 54.7), turned to 0 degrees
- moved JP1 146.9 mm to (141.2, 95.7), turned to 0 degrees
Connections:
- C37 pad 1: Net-(C37-Pad1) -> +12V
- C38 pad 1: Net-(C38-Pad1) -> +12V
- C39 pad 1: Net-(C38-Pad1) -> +12V
- D21 pad 2: +3V3 -> Net-(D21-Pad2)
- JP1 pad 1: +5V -> /orange_pi/OPI_USB-DM2
- JP1 pad 2: Net-(C37-Pad1) -> /orange_pi/USB-DM2
- JP2 pad 1: +3V3 -> /orange_pi/OPI_USB-DP2
- JP2 pad 2: Net-(C38-Pad1) -> /orange_pi/USB-DP2
- R65 pad 1: Net-(D21-Pad1) -> GND
- R65 pad 2: GND -> /FANS/FAN2/FAN_EN
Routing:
- net GND: track 22.2 -> 0.00 mm, vias 1 -> 0
- net Net-(C38-Pad1): track 21.4 -> 0.00 mm, vias 1 -> 0
- net Net-(C37-Pad1): track 13.7 -> 0.00 mm, vias 2 -> 0
- net +3V3: track 2.68 -> 0.00 mm
- net Net-(D21-Pad1): track 2.16 -> 0.00 mm, vias 1 -> 0
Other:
- board outline added: 100 x 100 mm
